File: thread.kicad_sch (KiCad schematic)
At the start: 18 parts, among them U301 nRF52840, Y301 32MHz

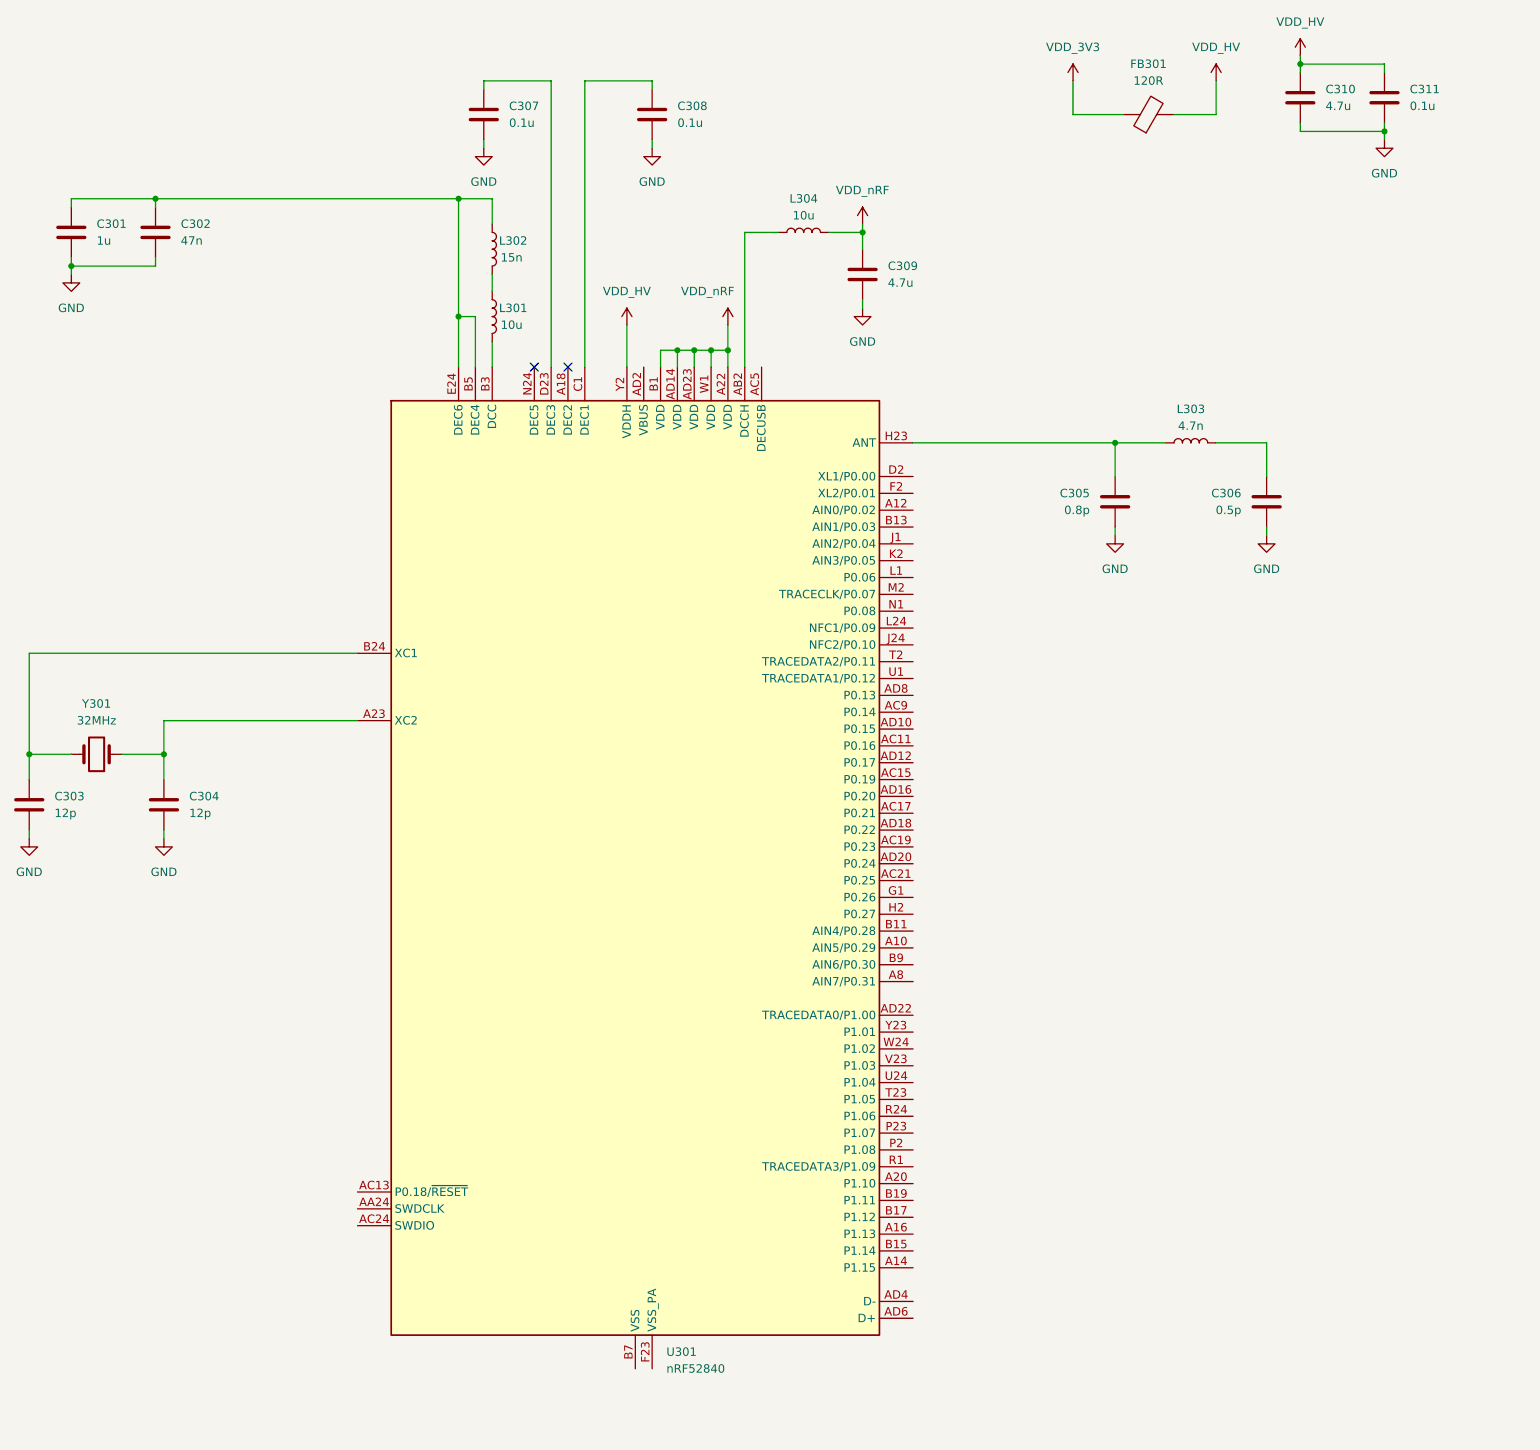
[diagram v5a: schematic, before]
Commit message: Added more thread circuitry
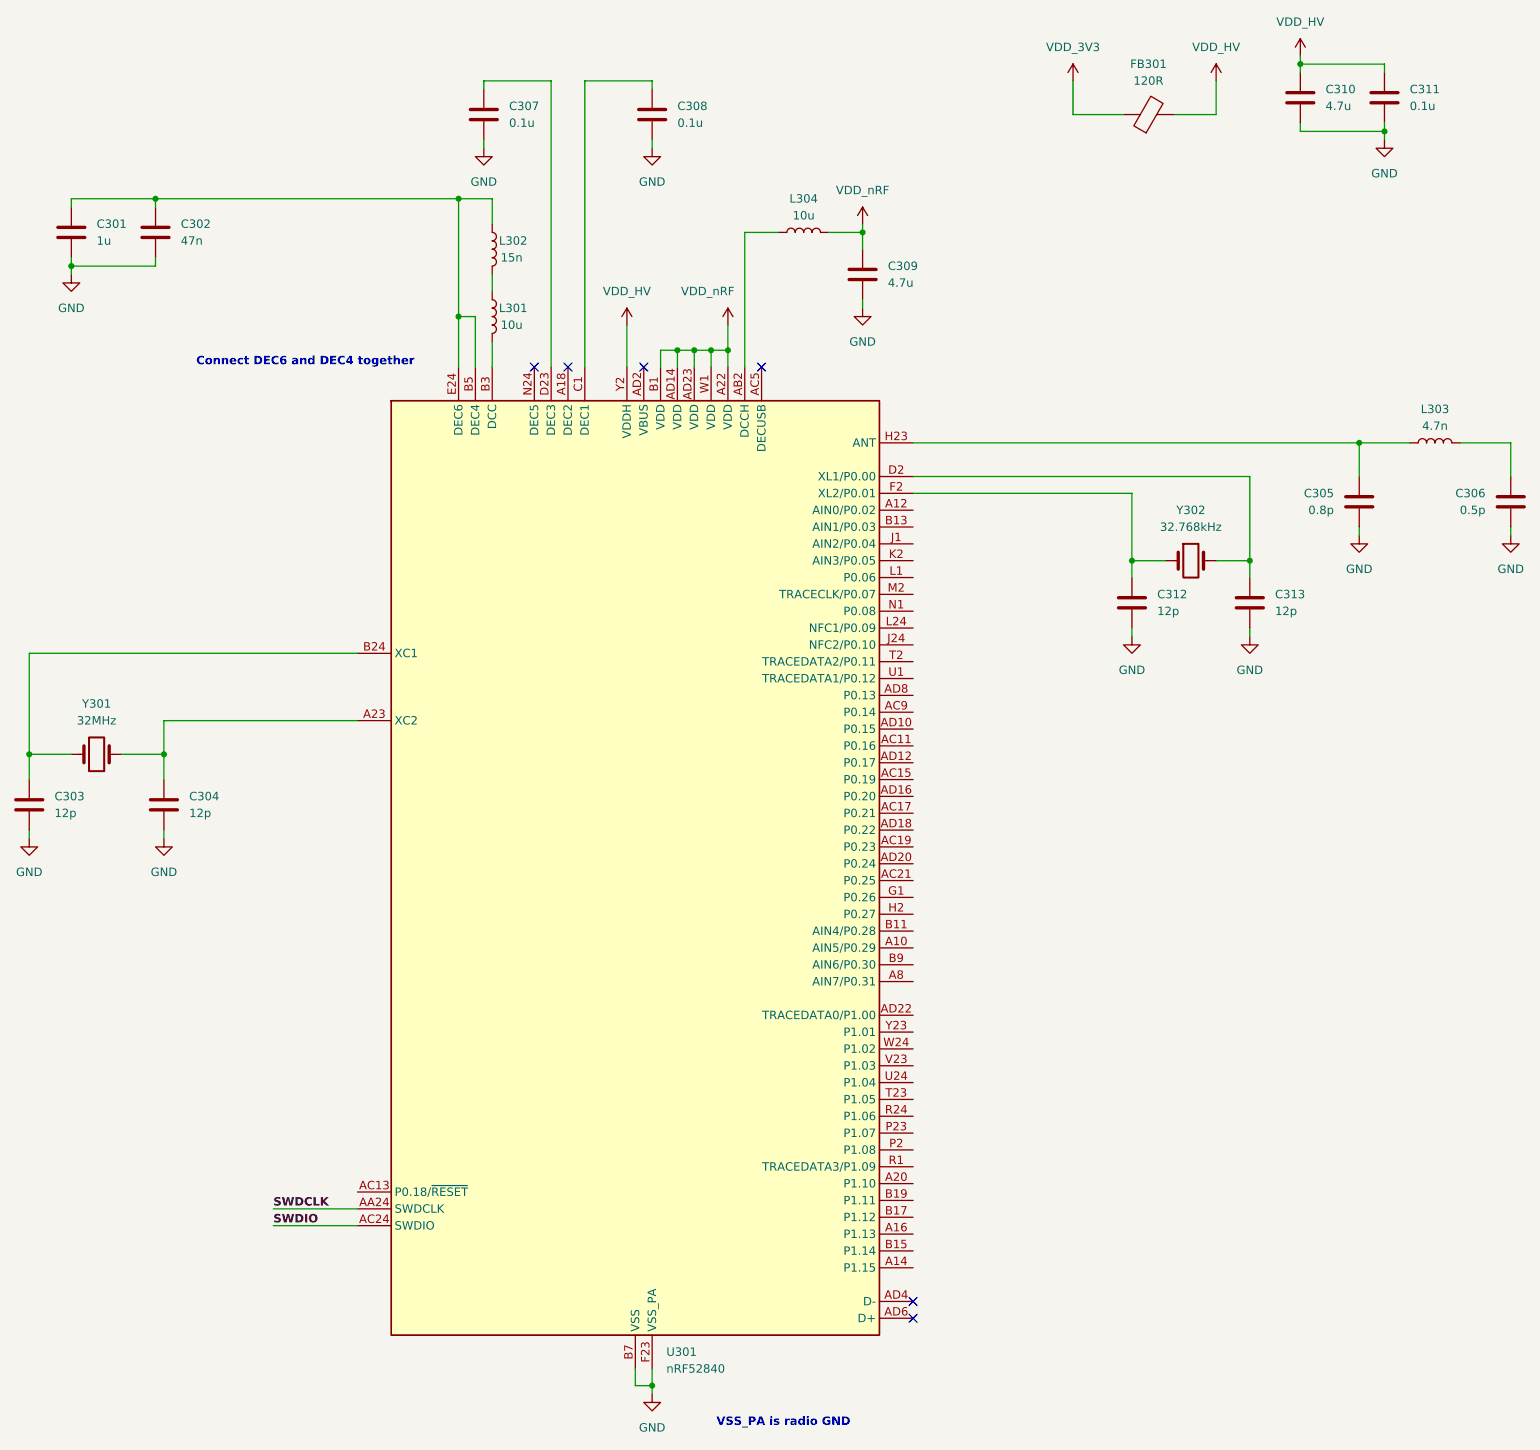
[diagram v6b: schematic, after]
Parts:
- added C312, C313: 12p, symbol Device:C
- added Y302: 32.768kHz, symbol Device:Crystal
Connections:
- net GND: now also U301.B7 (VSS), U301.EP (VSS), U301.F23 (VSS_PA), C312.2, C313.2
- net SWDCLK: now reaches U301.AA24 (SWDCLK)
- net SWDIO: now reaches U301.AC24 (SWDIO)
- net at U301.D2 (XL1/P0.00): now also C313.1, Y302.2
- net at U301.F2 (XL2/P0.01): now also C312.1, Y302.1
- no-connect marks 2 -> 6
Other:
- note added: "Connect DEC6 and DEC4 together"
- note added: "VSS_PA is radio GND"
- moved on the sheet: C305, C306, L303

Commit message: Added thread circuitry
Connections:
- net nRF_SPI0_MOSI: now reaches U301.AC9 (P0.14)
- net nRF_SPI0_MISO: now reaches U301.AD10 (P0.15)
- net nRF_SPI0_CLK: now reaches U301.AD8 (P0.13)
- net nRF_SPI0_CS0: now reaches U301.U1 (TRACEDATA1/P0.12)
- net SWDCLK renamed nRF_SWDCLK
- net SWDIO renamed nRF_SWDIO
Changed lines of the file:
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@@
+	(wire
+		(pts
+			(xy 193.04 147.32) (xy 204.47 147.32)
+		)
+		(stroke
+			(width 0)
+			(type default)
+		)
+	)
 	(wire
 		(pts
@@
 	(wire
 		(pts
+			(xy 193.04 149.86) (xy 204.47 149.86)
+		)
+		(stroke
+			(width 0)
+			(type default)
+		)
+	)
+	(wire
+		(pts
 			(xy 217.17 52.07) (xy 217.17 57.15)
 		)
@@
 	(wire
 		(pts
+			(xy 193.04 142.24) (xy 204.47 142.24)
+		)
+		(stroke
+			(width 0)
+			(type default)
+		)
+	)
+	(wire
+		(pts
 			(xy 260.35 106.68) (xy 267.97 106.68)
 		)
@@
 	(wire
 		(pts
-			(xy 96.52 222.25) (xy 109.22 222.25)
+			(xy 90.17 222.25) (xy 109.22 222.25)
 		)
 		(stroke
@@
 	(wire
 		(pts
+			(xy 193.04 144.78) (xy 204.47 144.78)
+		)
+		(stroke
+			(width 0)
+			(type default)
+		)
+	)
+	(wire
+		(pts
 			(xy 165.1 88.9) (xy 165.1 92.71)
 		)
@@
 	(wire
 		(pts
-			(xy 96.52 224.79) (xy 109.22 224.79)
+			(xy 90.17 224.79) (xy 109.22 224.79)
 		)
 		(stroke
@@
 		)
 	)
-	(label "SWDIO"
-		(at 96.52 224.79 0)
+	(label "nRF_SWDIO"
+		(at 90.17 224.79 0)
 		(effects
 			(font
@@
 		)
 	)
-	(label "SWDCLK"
-		(at 96.52 222.25 0)
+	(label "nRF_SWDCLK"
+		(at 90.17 222.25 0)
 		(effects
 			(font
@@
 		)
 	)
+	(global_label "nRF_SPI0_CLK"
+		(shape input)
+		(at 204.47 144.78 0)
+		(fields_autoplaced yes)
+		(effects
+			(font
+				(size 1.27 1.27)
+			)
+			(justify left)
+		)
+		(property "Intersheetrefs" "${INTERSHEET_REFS}"
+			(at 220.7599 144.78 0)
+			(effects
+				(font
+					(size 1.27 1.27)
+				)
+				(justify left)
+				(hide yes)
+			)
+		)
+	)
+	(global_label "nRF_SPI0_MOSI"
+		(shape input)
+		(at 204.47 147.32 0)
+		(fields_autoplaced yes)
+		(effects
+			(font
+				(size 1.27 1.27)
+			)
+			(justify left)
+		)
+		(property "Intersheetrefs" "${INTERSHEET_REFS}"
+			(at 221.788 147.32 0)
+			(effects
+				(font
+					(size 1.27 1.27)
+				)
+				(justify left)
+				(hide yes)
+			)
+		)
+	)
+	(global_label "nRF_SPI0_CS0"
+		(shape input)
+		(at 204.47 142.24 0)
+		(fields_autoplaced yes)
+		(effects
+			(font
+				(size 1.27 1.27)
+			)
+			(justify left)
+		)
+		(property "Intersheetrefs" "${INTERSHEET_REFS}"
+			(at 220.8808 142.24 0)
+			(effects
+				(font
+					(size 1.27 1.27)
+				)
+				(justify left)
+				(hide yes)
+			)
+		)
+	)
+	(global_label "nRF_SPI0_MISO"
+		(shape input)
+		(at 204.47 149.86 0)
+		(fields_autoplaced yes)
+		(effects
+			(font
+				(size 1.27 1.27)
+			)
+			(justify left)
+		)
+		(property "Intersheetrefs" "${INTERSHEET_REFS}"
+			(at 221.788 149.86 0)
+			(effects
+				(font
+					(size 1.27 1.27)
+				)
+				(justify left)
+				(hide yes)
+			)
+		)
+	)

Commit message: Fixed SoC power circuitry
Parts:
- renumbered C310 to C3001, C311 to C3002, C307 to C3003, C308 to C3004, C301 to C3005, C302 to C3006, C309 to C3007, C305 to C3008, C306 to C3009, C312 to C3010, C313 to C3011, C303 to C3012, C304 to C3013, FB301 to FB3001, L304 to L3001, L302 to L3002, L301 to L3003, L303 to L3004, U301 to U3001, Y302 to Y3001, Y301 to Y3002
